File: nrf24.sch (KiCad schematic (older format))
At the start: 1 part

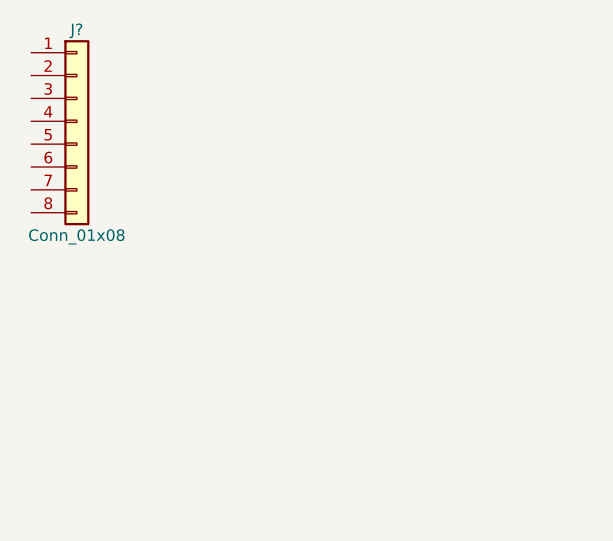
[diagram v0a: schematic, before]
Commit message: completed schematic and netlist
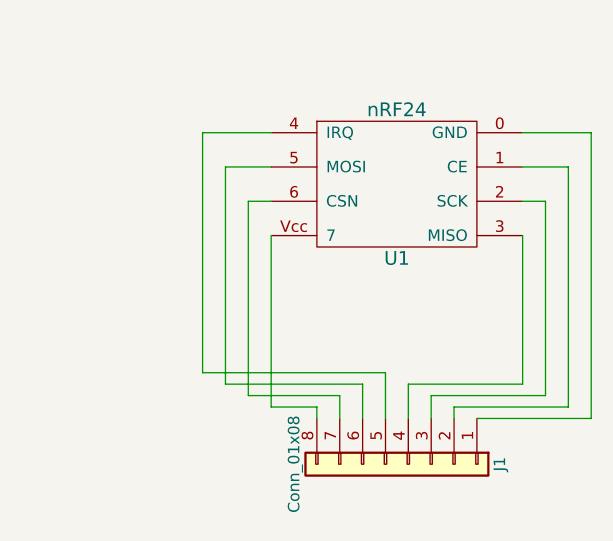
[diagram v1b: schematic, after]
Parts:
- added U1: nRF24, nrf_footprints:nrf24_footprint, symbol nRF24
- J1: renamed from J?; footprint (none) -> Pin_Headers:Pin_Header_Straight_1x08_Pitch2.54mm
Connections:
- net at J1.1 (Pin_1): now also U1.0 (GND)
- net at J1.2 (Pin_2): now also U1.1 (CE)
- net at J1.3 (Pin_3): now also U1.2 (SCK)
- net at J1.4 (Pin_4): now also U1.3 (MISO)
- net at J1.5 (Pin_5): now also U1.4 (IRQ)
- net at J1.6 (Pin_6): now also U1.5 (MOSI)
- net at J1.7 (Pin_7): now also U1.6 (CSN)
- net at J1.8 (Pin_8): now also U1.Vcc (7)
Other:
- moved on the sheet: J1
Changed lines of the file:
@@
 LIBS:contrib
 LIBS:valves
+LIBS:nrf24_schematic_library
 EELAYER 25 0
 EELAYER END
@@
 $EndDescr
 $Comp
-L Conn_01x08 J?
+L Conn_01x08 J1
 U 1 1 5A2326F0
-P 4250 3350
-F 0 "J?" H 4250 3750 50  0000 C CNN
-F 1 "Conn_01x08" H 4250 2850 50  0000 C CNN
-F 2 "" H 4250 3350 50  0001 C CNN
-F 3 "" H 4250 3350 50  0001 C CNN
-	1    4250 3350
+P 5700 4850
+F 0 "J1" H 5700 5250 50  0000 C CNN
+F 1 "Conn_01x08" H 5700 4350 50  0000 C CNN
+F 2 "Pin_Headers:Pin_Header_Straight_1x08_Pitch2.54mm" H 5700 4850 50  0001 C CNN
+F 3 "" H 5700 4850 50  0001 C CNN
+	1    5700 4850
+	0    1    1    0
+$EndComp
+$Comp
+L nRF24 U1
+U 1 1 5A28B150
+P 5650 3650
+F 0 "U1" H 5650 3350 60  0000 C CNN
+F 1 "nRF24" H 5650 4000 60  0000 C CNN
+F 2 "nrf_footprints:nrf24_footprint" H 5650 3650 60  0001 C CNN
+F 3 "" H 5650 3650 60  0001 C CNN
+	1    5650 3650
 	1    0    0    -1
 $EndComp
+Wire Wire Line
+	6200 3400 6500 3400
+Wire Wire Line
+	6500 3400 6500 4650
+Wire Wire Line
+	6500 4650 6000 4650
+Wire Wire Line
+	6200 3550 6400 3550
+Wire Wire Line
+	6400 3550 6400 4600
+Wire Wire Line
+	6400 4600 5900 4600
+Wire Wire Line
+	5900 4600 5900 4650
+Wire Wire Line
+	6200 3700 6300 3700
+Wire Wire Line
+	6300 3700 6300 4550
+Wire Wire Line
+	6300 4550 5800 4550
+Wire Wire Line
+	5800 4550 5800 4650
+Wire Wire Line
+	6200 3850 6200 4500
+Wire Wire Line
+	6200 4500 5700 4500
+Wire Wire Line
+	5700 4500 5700 4650
+Wire Wire Line
+	5100 3850 5100 4600
+Wire Wire Line
+	5100 4600 5300 4600
+Wire Wire Line
+	5300 4600 5300 4650
+Wire Wire Line
+	5100 3700 5000 3700
+Wire Wire Line
+	5000 3700 5000 4550
+Wire Wire Line
+	5000 4550 5400 4550
+Wire Wire Line
+	5400 4550 5400 4650
+Wire Wire Line
+	5100 3550 4900 3550
+Wire Wire Line
+	4900 3550 4900 4500
+Wire Wire Line
+	4900 4500 5500 4500
+Wire Wire Line
+	5500 4500 5500 4650
+Wire Wire Line
+	5100 3400 4800 3400
+Wire Wire Line
+	4800 3400 4800 4450
+Wire Wire Line
+	4800 4450 5600 4450
+Wire Wire Line
+	5600 4450 5600 4650
 $EndSCHEMATC

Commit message: Fix an incorrect pin assignment in nrf24 schematic component
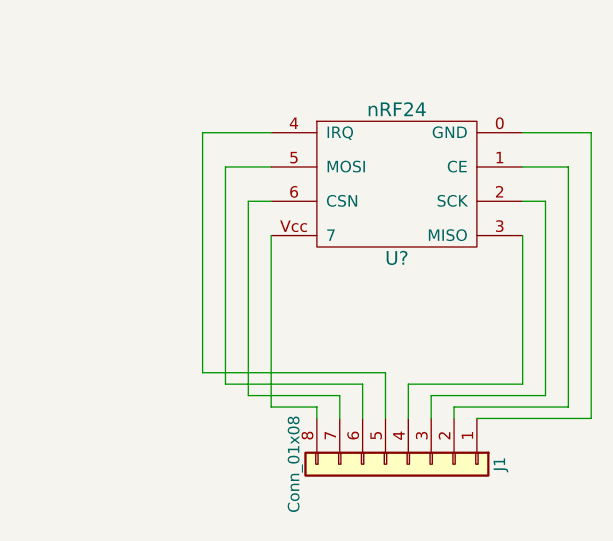
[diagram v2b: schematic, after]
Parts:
- removed U1: nRF24, nrf_footprints:nrf24_footprint, symbol nRF24
- added U?: nRF24, symbol nRF24
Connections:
- net at J1.1 (Pin_1): now also U?.0 (GND)
- net at J1.2 (Pin_2): now also U?.1 (CE)
- net at J1.3 (Pin_3): now also U?.2 (SCK)
- net at J1.4 (Pin_4): now also U?.3 (MISO)
- net at J1.5 (Pin_5): now also U?.4 (IRQ)
- net at J1.6 (Pin_6): now also U?.5 (MOSI)
- net at J1.7 (Pin_7): now also U?.6 (CSN)
- net at J1.8 (Pin_8): now also U?.Vcc (7)
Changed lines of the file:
@@
 LIBS:valves
 LIBS:nrf24_schematic_library
+LIBS:nrf24-cache
 EELAYER 25 0
 EELAYER END
@@
 	1    5700 4850
 	0    1    1    0
-$EndComp
-$Comp
-L nRF24 U1
-U 1 1 5A28B150
-P 5650 3650
-F 0 "U1" H 5650 3350 60  0000 C CNN
-F 1 "nRF24" H 5650 4000 60  0000 C CNN
-F 2 "nrf_footprints:nrf24_footprint" H 5650 3650 60  0001 C CNN
-F 3 "" H 5650 3650 60  0001 C CNN
-	1    5650 3650
-	1    0    0    -1
 $EndComp
 Wire Wire Line
@@
 Wire Wire Line
 	5600 4450 5600 4650
+$Comp
+L nRF24 U?
+U 1 1 5A2E002F
+P 5650 3650
+F 0 "U?" H 5650 3350 60  0000 C CNN
+F 1 "nRF24" H 5650 4000 60  0000 C CNN
+F 2 "" H 5650 3650 60  0001 C CNN
+F 3 "" H 5650 3650 60  0001 C CNN
+	1    5650 3650
+	1    0    0    -1
+$EndComp
 $EndSCHEMATC

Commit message: Initial layout
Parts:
- U1: renamed from U?; footprint (none) -> nrf_footprints:nrf24_footprint
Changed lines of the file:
@@
 	5600 4450 5600 4650
 $Comp
-L nRF24 U?
+L nRF24 U1
 U 1 1 5A2E002F
 P 5650 3650
-F 0 "U?" H 5650 3350 60  0000 C CNN
+F 0 "U1" H 5650 3350 60  0000 C CNN
 F 1 "nRF24" H 5650 4000 60  0000 C CNN
-F 2 "" H 5650 3650 60  0001 C CNN
+F 2 "nrf_footprints:nrf24_footprint" H 5650 3650 60  0001 C CNN
 F 3 "" H 5650 3650 60  0001 C CNN
 	1    5650 3650

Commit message: final layout and gerber files
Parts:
- added C1: 10uF, Capacitors_THT:CP_Radial_D10.0mm_P5.00mm, symbol CP
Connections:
- wire segments 29 -> 31
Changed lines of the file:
@@
 LIBS:valves
 LIBS:nrf24_schematic_library
-LIBS:nrf24-cache
 EELAYER 25 0
 EELAYER END
@@
 	1    0    0    -1
 $EndComp
+$Comp
+L CP C1
+U 1 1 5A2F5C2C
+P 5600 4250
+F 0 "C1" H 5625 4350 50  0000 L CNN
+F 1 "10uF" H 5625 4150 50  0000 L CNN
+F 2 "Capacitors_THT:CP_Radial_D10.0mm_P5.00mm" H 5638 4100 50  0001 C CNN
+F 3 "" H 5600 4250 50  0001 C CNN
+	1    5600 4250
+	0    -1   -1   0
+$EndComp
+Wire Wire Line
+	5750 4250 6500 4250
+Connection ~ 6500 4250
+Wire Wire Line
+	5450 4250 5100 4250
+Connection ~ 5100 4250
 $EndSCHEMATC
